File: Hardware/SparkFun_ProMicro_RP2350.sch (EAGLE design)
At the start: 60 parts, among them J2 QWIIC_RIGHT_ANGLE, J5 USB Female Type C Connector, U1 3.3V, U2 RP2350A, U3 WS2812-2020, U4 W25QXX128MBIT, Y1 12MHz

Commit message: Cleanup
Rename design files
Change version number to v01
Update attributions
Update silk name
Update ordering instructions
Update measures
Update SPI data net names to POCI and PICO
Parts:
- FRAME2: DESIGNER (none) -> Dryw Wade; REV (none) -> v01
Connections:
- net 20/SPI_CIPO renamed 20/SPI_POCI
- net 23/SPI_COPI renamed 23/SPI_PICO
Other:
- note added: "Based on design by: Nathan Seidle"
- note removed: "v11"
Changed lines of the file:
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@@
 <part name="U3" library="SparkFun-LED" deviceset="WS2812-2020" device=""/>
 <part name="GND4" library="SparkFun-PowerSymbols" deviceset="GND" device=""/>
-<part name="FRAME2" library="SparkFun-Aesthetics" deviceset="FRAME-LEDGER" device=""/>
+<part name="FRAME2" library="SparkFun-Aesthetics" deviceset="FRAME-LEDGER" device="">
+<attribute name="DESIGNER" value="Dryw Wade"/>
+<attribute name="REV" value="v01"/>
+</part>
 <part name="TP3" library="SparkFun-Connectors" deviceset="TEST-POINT" device="3X5" value="TEST-POINT3X5"/>
 <part name="U2" library="RP2350A" deviceset="RP2350A" device=""/>
@@
 <text x="287.02" y="220.98" size="1.778" layer="97" align="center">Max Voltage Input: 5.3VDC</text>
 <text x="287.02" y="218.44" size="1.778" layer="97" align="center">Max Current Output: 600mA</text>
-<text x="421.64" y="7.62" size="2.54" layer="94">v11</text>
 <text x="76.454" y="266.446" size="2.54" layer="94" font="vector" align="center">Raspberry Pi RP2350</text>
 <text x="178.054" y="256.286" size="2.54" layer="94" font="vector" align="center">16MB Flash</text>
@@
 V-Reg can handle up to 6V
 but WS2812 max is 5.3V</text>
+<text x="331.724" y="6.604" size="2.54" layer="94" font="vector">Based on design by: Nathan Seidle</text>
 </plain>
 <instances>
@@
 </segment>
 </net>
-<net name="23/SPI_COPI" class="0">
+<net name="23/SPI_PICO" class="0">
 <segment>
 <wire x1="96.52" y1="193.04" x2="99.06" y2="193.04" width="0.1524" layer="91"/>
@@
 </segment>
 </net>
-<net name="20/SPI_CIPO" class="0">
+<net name="20/SPI_POCI" class="0">
 <segment>
 <wire x1="96.52" y1="200.66" x2="99.06" y2="200.66" width="0.1524" layer="91"/>

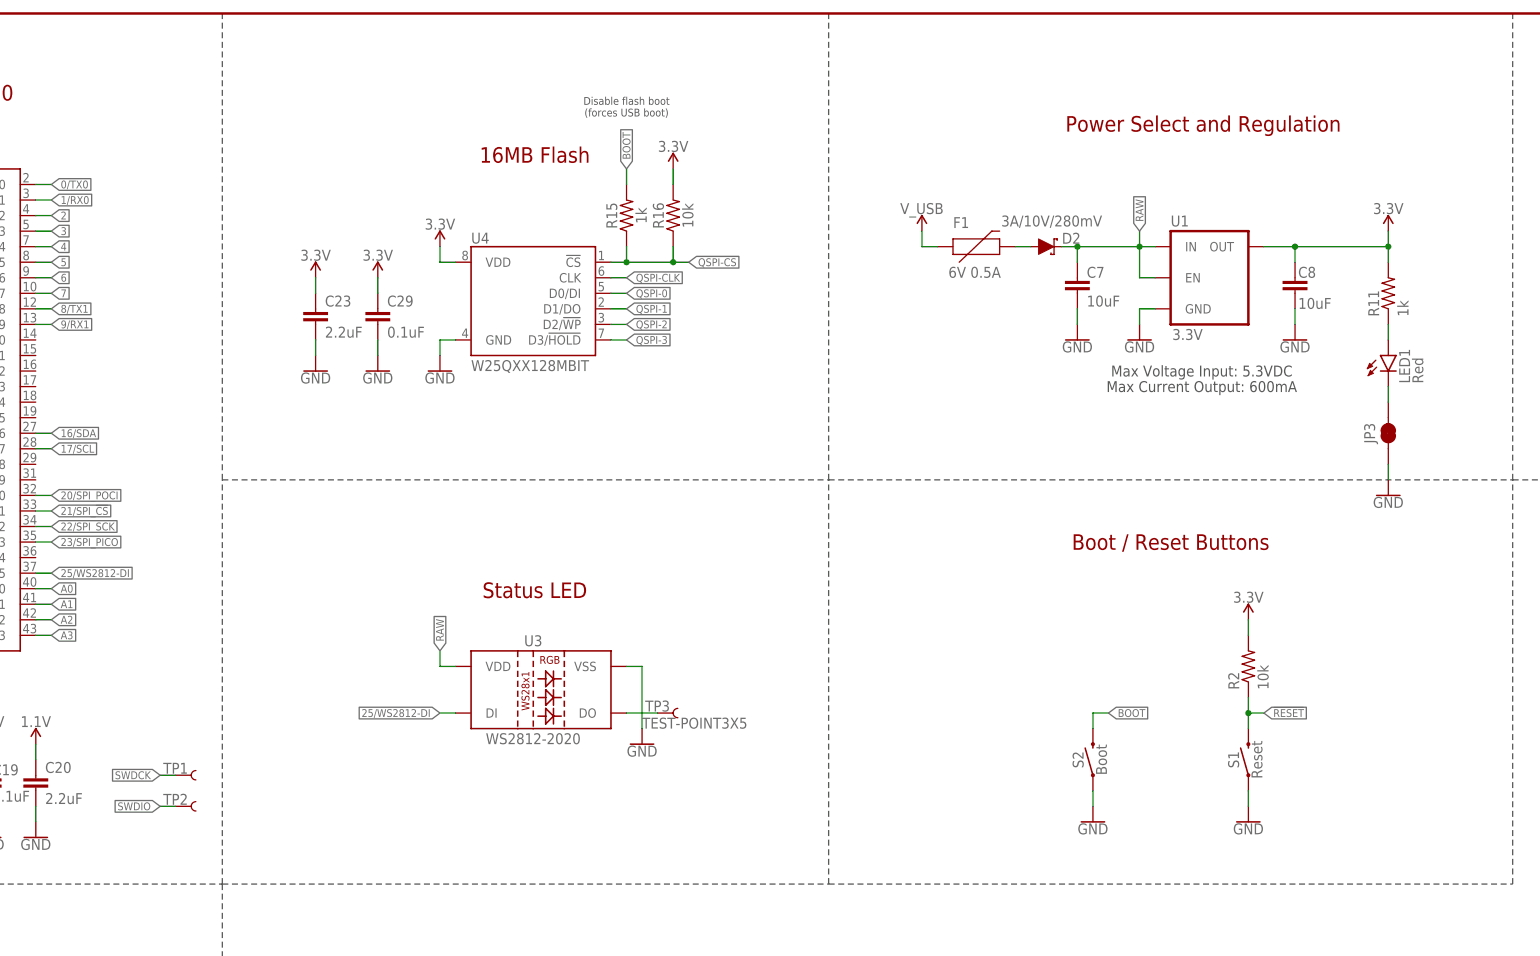
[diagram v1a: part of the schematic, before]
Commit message: More cleanup
Add test point for BOOT net
Nudge a few traces and vias to improve copper pours
Approve DRC errors
Fix traces overlapping vias
Fix acid traps
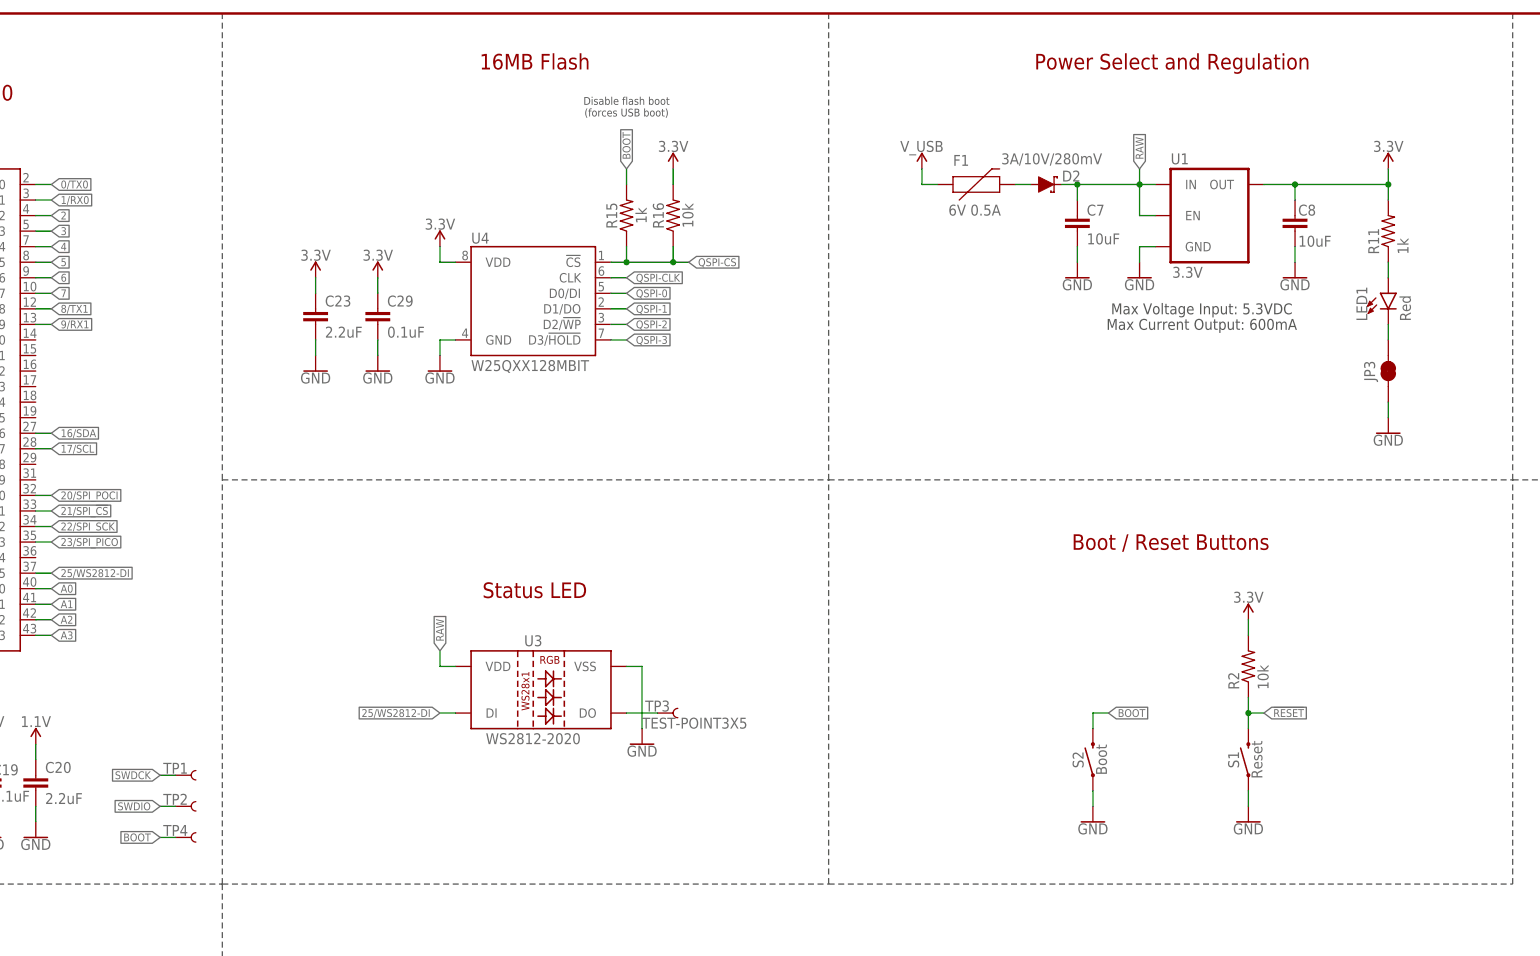
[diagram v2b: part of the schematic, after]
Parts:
- added TP4: TEST-POINT3X5, SparkFun-Connectors:TEST-POINT3X5
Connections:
- net BOOT: now also TP4.1
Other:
- moved on the sheet: C7, C8, D2, F1, JP3, LED1, R11, U1

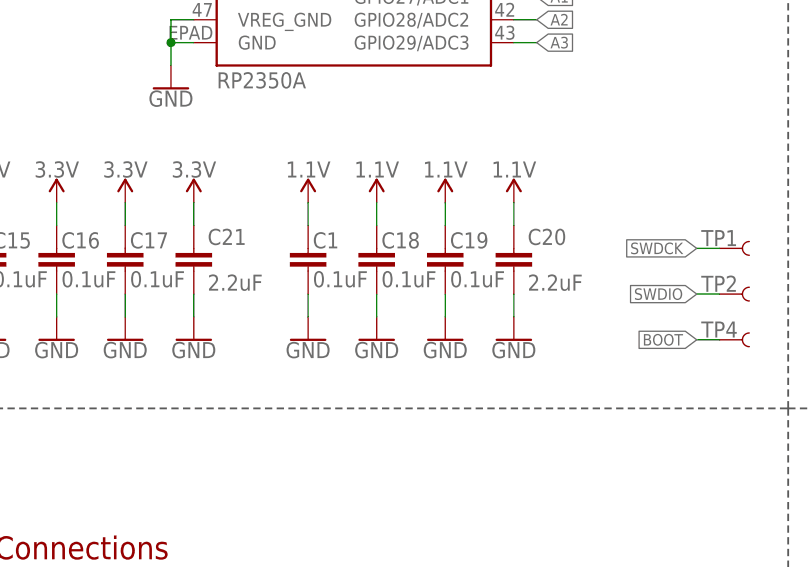
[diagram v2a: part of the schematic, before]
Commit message: Change C20 and C21 from 2.2uF to 10uF
Recommended by hardware guidelines
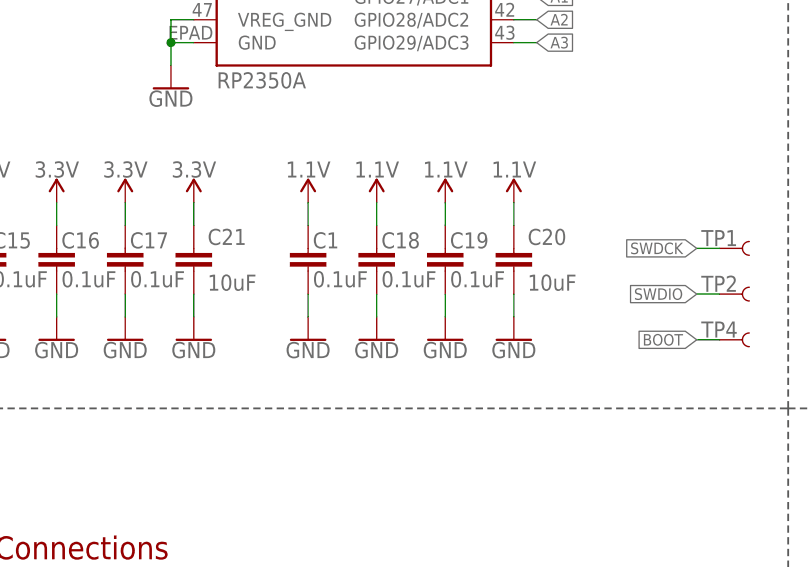
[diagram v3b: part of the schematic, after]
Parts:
- C20, C21: value 2.2uF -> 10uF; device SparkFun-Capacitors:2.2UF-0402_TIGHT-10V-10%-X5R -> SparkFun-Capacitors:10UF-0402T-6.3V-20%
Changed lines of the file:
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@@
 <part name="SUPPLY25" library="RP2040" deviceset="1.1V" device=""/>
 <part name="SUPPLY26" library="RP2040" deviceset="1.1V" device=""/>
-<part name="C20" library="SparkFun-Capacitors" deviceset="2.2UF" device="-0402_TIGHT-10V-10%-X5R" value="2.2uF"/>
-<part name="C21" library="SparkFun-Capacitors" deviceset="2.2UF" device="-0402_TIGHT-10V-10%-X5R" value="2.2uF"/>
+<part name="C20" library="SparkFun-Capacitors" deviceset="10UF" device="-0402T-6.3V-20%" value="10uF"/>
+<part name="C21" library="SparkFun-Capacitors" deviceset="10UF" device="-0402T-6.3V-20%" value="10uF"/>
 <part name="SUPPLY27" library="SparkFun-PowerSymbols" deviceset="3.3V" device=""/>
 <part name="SUPPLY28" library="RP2040" deviceset="1.1V" device=""/>

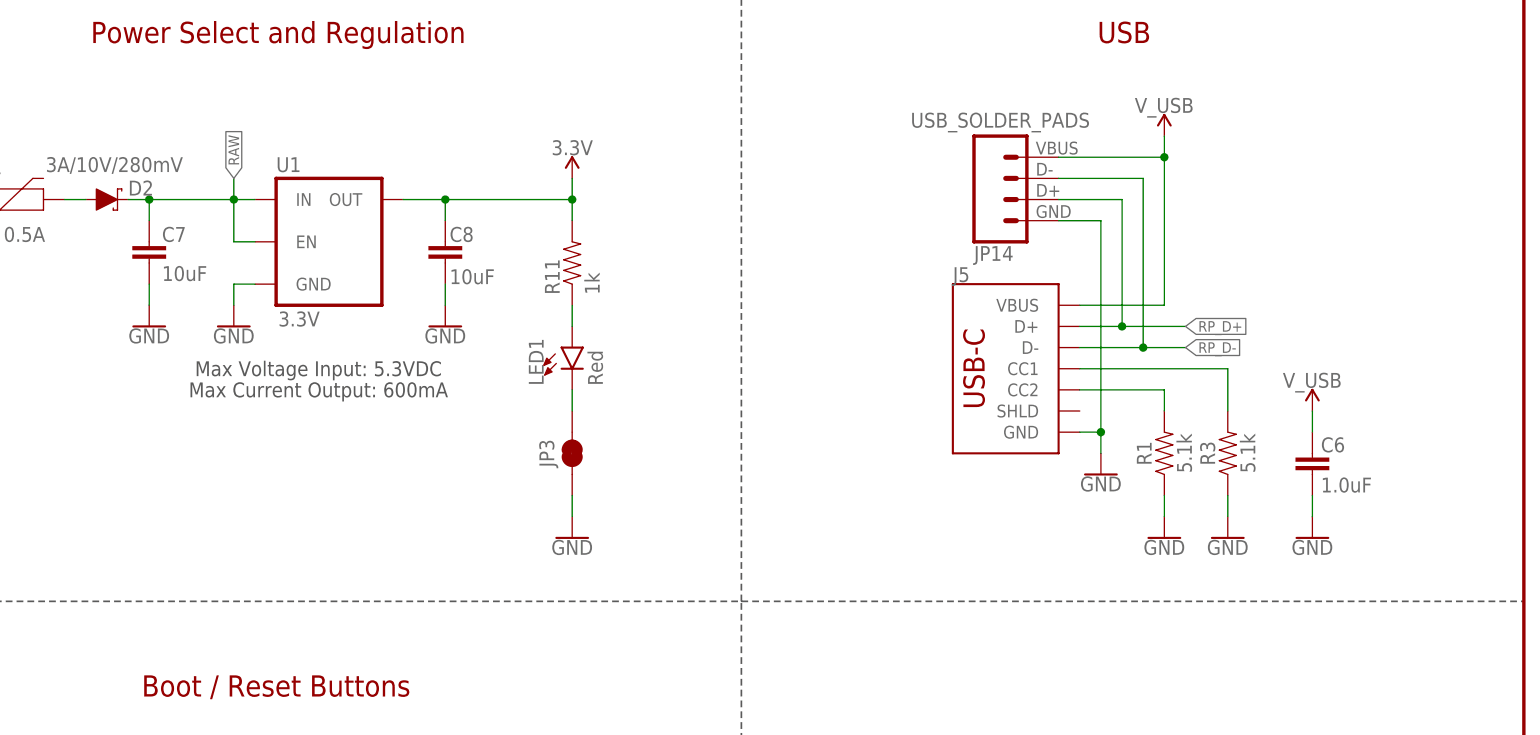
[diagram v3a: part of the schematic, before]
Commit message: Design review updates
Change regulator to RT9080
Add USB shield jumper and polygon to connect USB shield pads
Change PWR jumper silk to just be "P" and orient at 90 with silk polygon to connect it
Remove C6
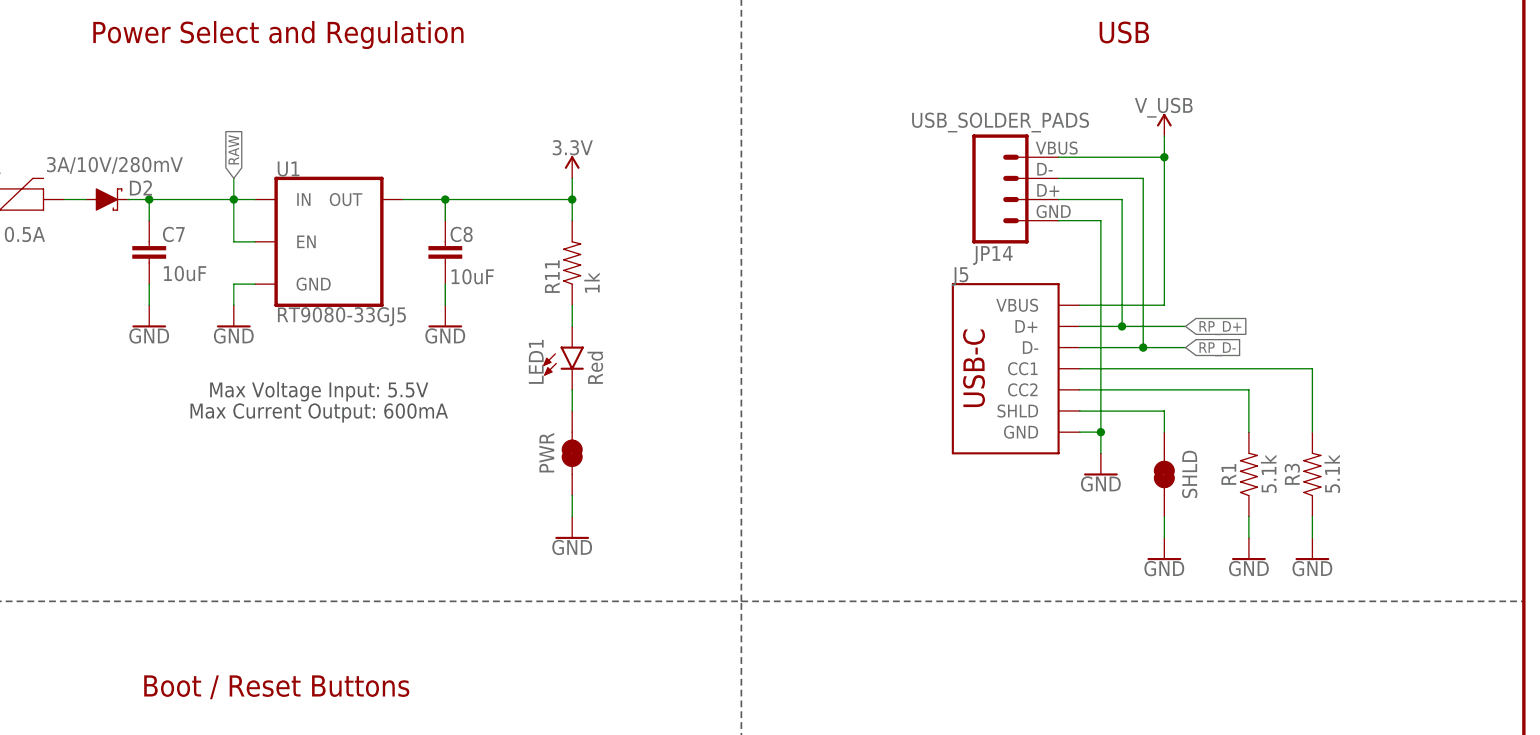
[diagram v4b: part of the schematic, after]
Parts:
- removed C6: 1.0uF, SparkFun-Capacitors:1.0UF-0402T-16V-10%
- added SHLD: JUMPER-SMT_2_NC_TRACE_SILK, SparkFun-Jumpers:JUMPER-SMT_2_NC_TRACE_SILK
- U1: value 3.3V -> RT9080-33GJ5; device SparkFun-IC-Power:V_REG_AP2112K-3.3V -> SparkFun-IC-Power:V_REG_RT9080
- renumbered JP3 to PWR
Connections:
- new net SHLD: J5.SHLD, SHLD.1
- net GND: now also SHLD.2; no longer C6.1
- net V_USB: no longer C6.2
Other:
- note added: "Max Voltage Input: 5.5V"
- note removed: "Max Voltage Input: 5.3VDC"
- moved on the sheet: R1, R3

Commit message: Clean up schematic
Rearrange sections to use whole frame
Update section titles
Move power LED and Qwiic connector to their own sections
Add text to jumpers indicating their functions
Change power LED to new version and update resistor
Swap VREG_AVDD and VREG_VIN pins on RP235 symbol to give more space for inductor in schematic
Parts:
- L1: value 4.7μH_SHIELDED_INDUCTOR -> 4.7μH
- LED1: device SparkFun-LED:LED-RED0603 -> SparkFun-LED:LED-RED_0603-KB
- R11: value 1k -> 4.7k; device SparkFun-Resistors:1KOHM-0402T-1/16W-1% -> SparkFun-Resistors:4.7KOHM-0402T-1/16W-1%
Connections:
- net N$1 renamed LED_OUT
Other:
- note added: "Castellated Headers"
- note added: "Cut PWR jumper (labelled "P" in silkscreen) to disconnect power LED"
- note added: "Cut SHLD jumper to disconnect USB shield from GND"
- note added: "Max Voltage on RAW: 5.3V V-Reg can handle up to 5.5V but WS2812 max is 5.3V"
- note added: "Power LED"
- note added: "Power Select and 3.3V Regulator - RT9080"
- note added: "Qwiic Connector and I2C Pullups"
- note added: "Test Points"
- note added: "USB-C Connector and USB Pads"
- note removed: "Connections"
- note removed: "Max Voltage on RAW: 5.3V V-Reg can handle up to 6V but WS2812 max is 5.3V"
- note removed: "Power Select and Regulation"
- note removed: "USB"
- moved on the sheet: C1, C11, C12, C13, C14, C15, C16, C17, C18, C19, C2, C20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
